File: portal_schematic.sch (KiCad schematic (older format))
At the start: 93 parts, among them J1 RS485_1, J2 ATX_PW_SW, J3 Sensor, J4 RS485_1_Config, J5 CAM_SW, J6 ILLUM_SW, J7 RS232_1, J8 RS232_2, K1 Relay_PW_SW, P1 Power, P10 CONN_01X01, P11 CONN_01X01, P12 CONN_01X01, P13 CONN_01X01, P2 Analog, P3 Analog, P4 Digital, P5 PWM, P6 PWM, P7 Communication, P8 CONN_01X01, P9 CONN_01X01, Q1 BSS123LT1, Q10 FDN340P, Q11 FDN340P, Q2 STP16NF06L, Q3 STP16NF06L, Q4 FDN340P, Q5 FDN340P, Q6 FDN340P, Q7 FDN340P, Q8 FDN340P, Q9 FDN340P, SW1 SW_UART1, U1 LTV-817S, U2 LTV-817S, U3 MAX481E, U4 MP1584, U5 LTV-817S, U6 LTV-817S, U7 MAX3232

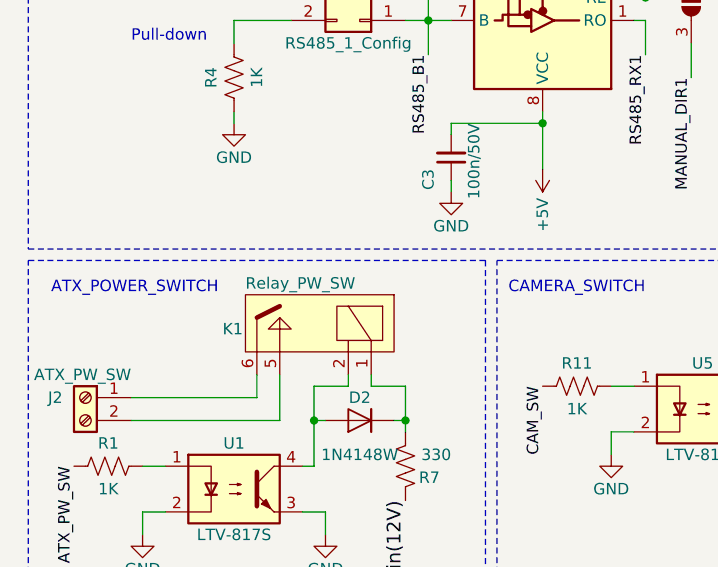
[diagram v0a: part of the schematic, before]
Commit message: Modified: visual enhancement is added
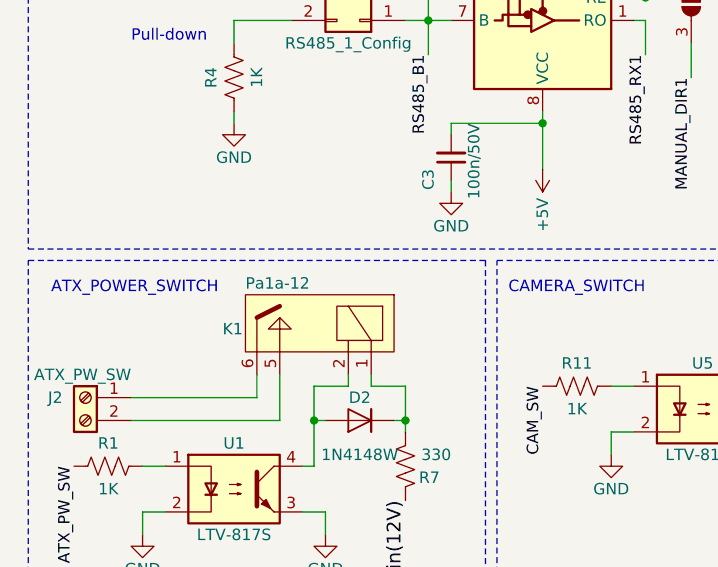
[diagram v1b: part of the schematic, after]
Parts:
- K1: value Relay_PW_SW -> Pa1a-12
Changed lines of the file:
@@
 P 1800 3100
 F 0 "K1" H 2200 3200 50  0000 R CNN
-F 1 "Relay_PW_SW" H 2100 3400 50  0000 R CNN
+F 1 "Pa1a-12" H 2100 3400 50  0000 R CNN
 F 2 "Relay_Panasonic:Relay_Panasonic_PA1a_xx_DIP" H 1800 3100 50  0001 C CNN
 F 3 "" H 1800 3100 50  0001 C CNN

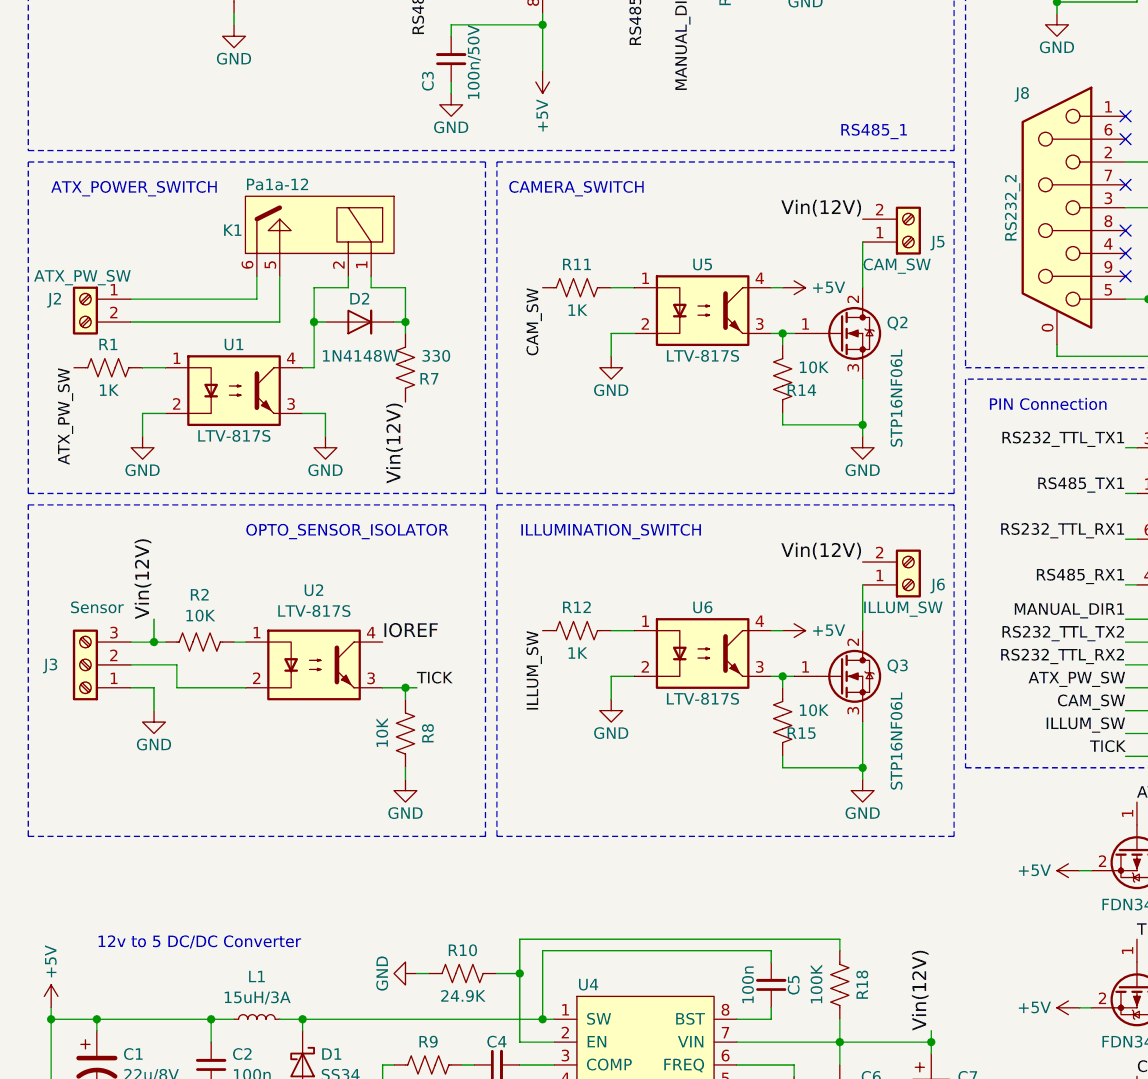
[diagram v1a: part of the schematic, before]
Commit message: The option of switching/powering in Cam and Illumination are added
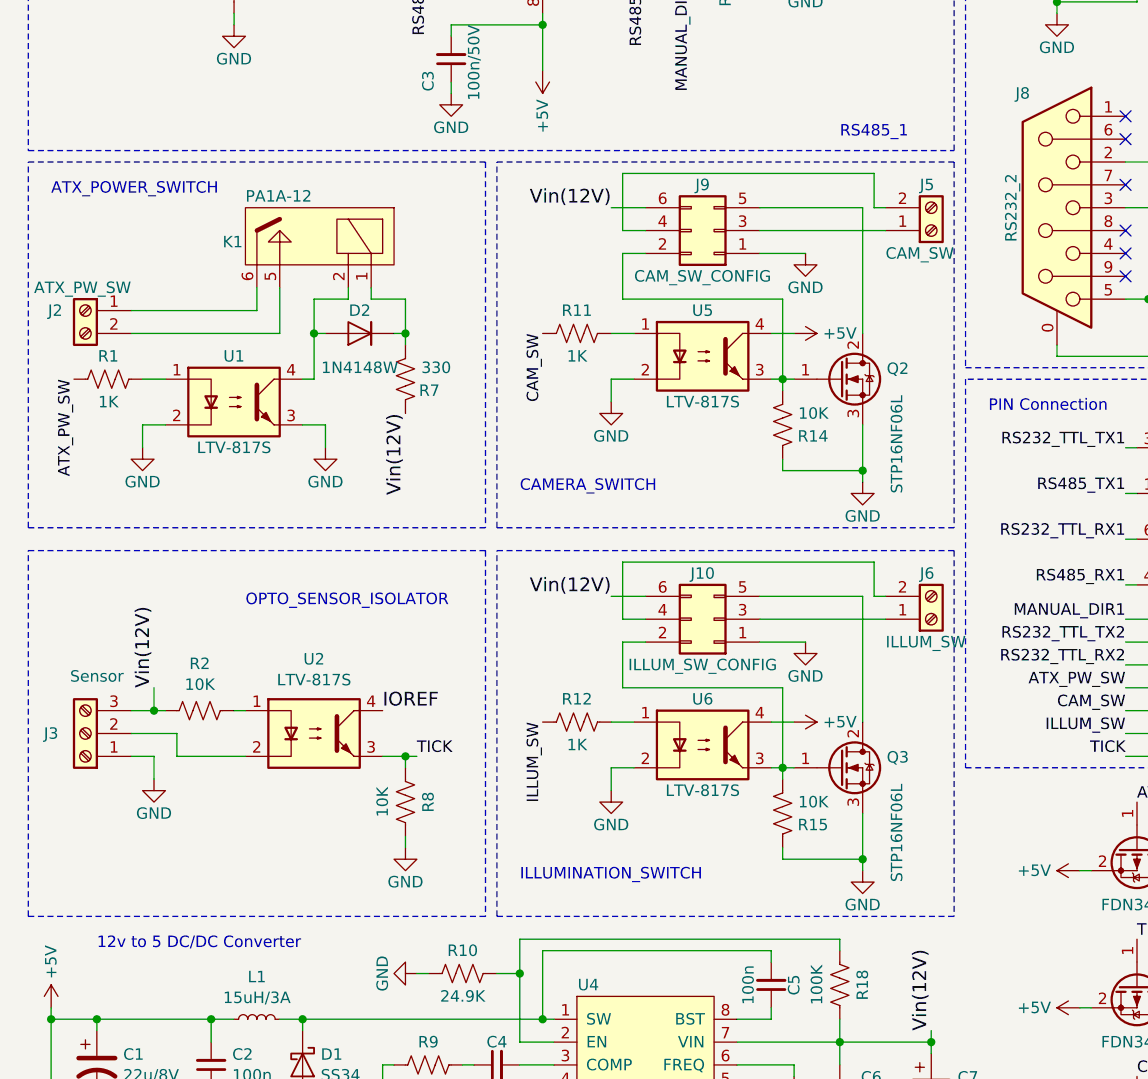
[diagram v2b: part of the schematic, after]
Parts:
- added J10: ILLUM_SW_CONFIG, Connector_PinHeader_2.54mm:PinHeader_2x03_P2.54mm_Vertical, symbol Connector_Generic:Conn_02x03_Odd_Even
- added J9: CAM_SW_CONFIG, Connector_PinHeader_2.54mm:PinHeader_2x03_P2.54mm_Vertical, symbol Connector_Generic:Conn_02x03_Odd_Even
- K1: value Pa1a-12 -> PA1A-12
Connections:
- net GND: now also J10.1 (Pin_1), J9.1 (Pin_1)
- net Vin(12V): now also J10.6 (Pin_6), J9.6 (Pin_6); no longer J5.2 (Pin_2), J6.2 (Pin_2)
- net at J5.1 (Pin_1): now also J9.3 (Pin_3); no longer Q2.2 (D)
- net at Q2.1 (G), R14.2, U5.3: now also J9.2 (Pin_2)
- net at J6.1 (Pin_1): now also J10.3 (Pin_3); no longer Q3.2 (D)
- net at Q3.1 (G), R15.2, U6.3: now also J10.2 (Pin_2)
- new net: J5.2 (Pin_2), J9.4 (Pin_4)
- new net: J9.5 (Pin_5), Q2.2 (D)
- new net: J10.4 (Pin_4), J6.2 (Pin_2)
- new net: J10.5 (Pin_5), Q3.2 (D)
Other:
- moved on the sheet: D2, J2, J3, J5, J6, K1, Q2, Q3, R1, R11, R12, R14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
